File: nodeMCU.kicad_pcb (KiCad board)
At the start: 2 copper layers, 25.4 x 48.3 mm, 34 parts, among them J1 USB_B_Micro, J2 Conn_01x15, J3 Conn_01x15, Q1 S8050, Q2 S8050, SW1 RESET, SW2 FLASH, U1 AP1117-33, U2 CP2102N-A01-GQFN28, U3 ESP-12E

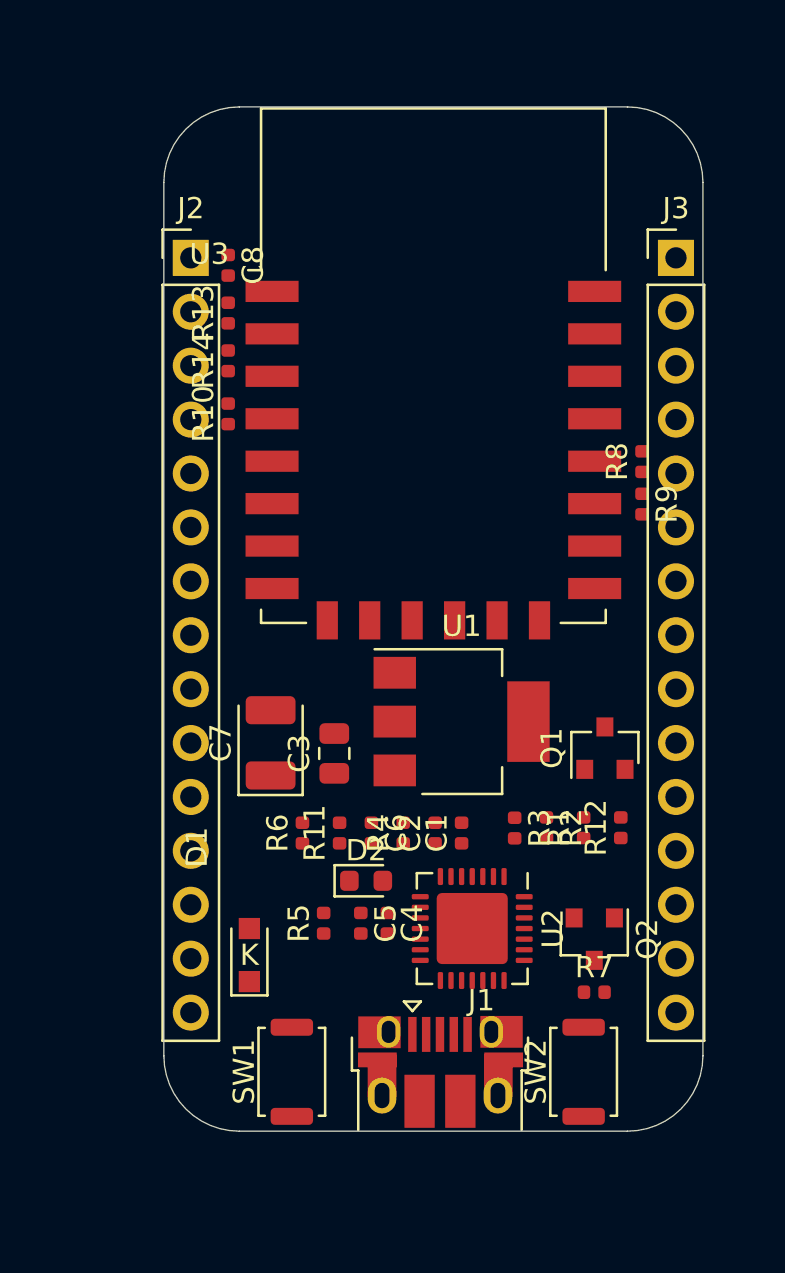
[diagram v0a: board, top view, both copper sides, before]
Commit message: Agrego agujeros de sujecion esquematico + pcb
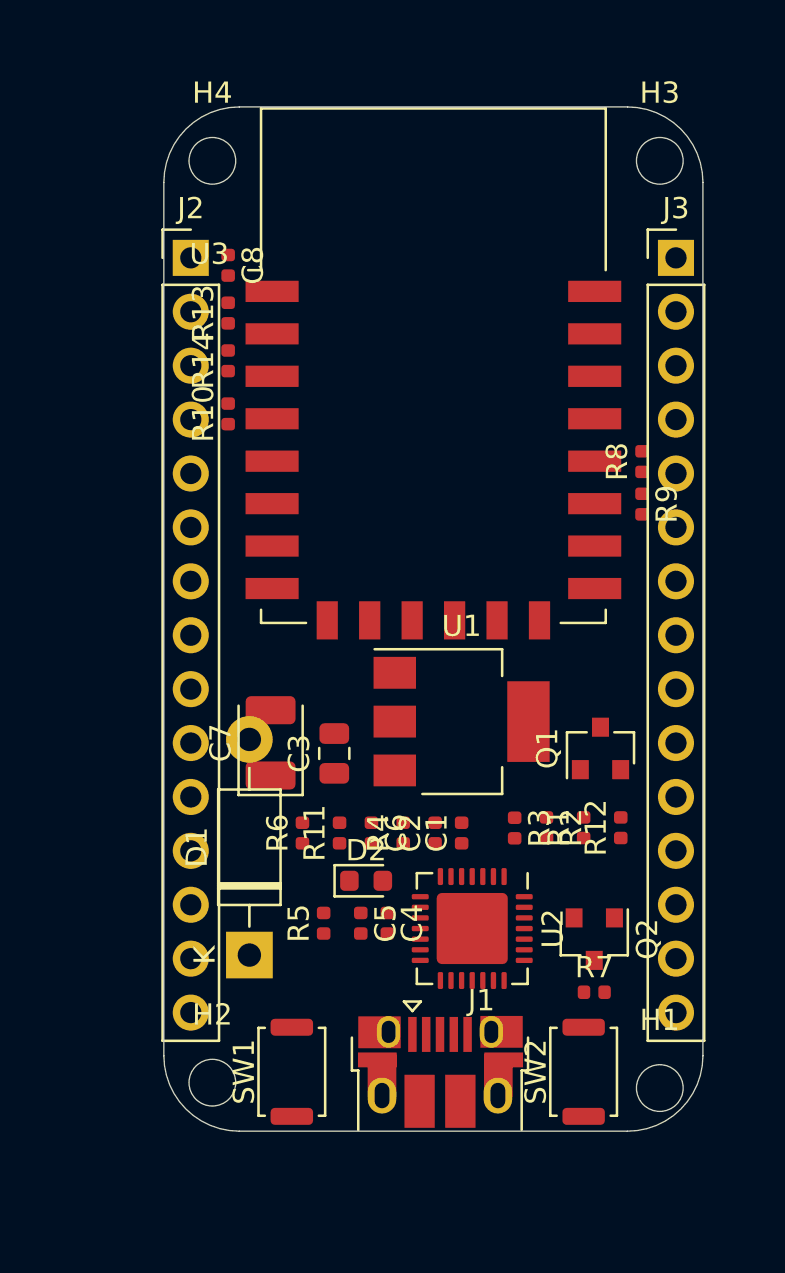
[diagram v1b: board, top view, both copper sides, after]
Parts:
- added H1: MountingHole, MountingHole:MountingHole_2.2mm_M2, F.Cu at (196.1, 96.3)
- added H2: MountingHole, MountingHole:MountingHole_2.2mm_M2, F.Cu at (175.0, 96.0)
- added H3: MountingHole, MountingHole:MountingHole_2.2mm_M2, F.Cu at (196.1, 52.6)
- added H4: MountingHole, MountingHole:MountingHole_2.2mm_M2, F.Cu at (175.0, 52.6)
- D1: footprint Diode_SMD:D_SOD-323_HandSoldering -> Diode_THT:D_DO-41_SOD81_P10.16mm_Horizontal
- moved Q1 0.21 mm to (193.3, 80.3)
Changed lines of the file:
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@@
     (tracks 0)
     (zones 0)
-    (modules 34)
+    (modules 38)
     (nets 56)
   )
@@
     )
   )
-  (module Diode_SMD:D_SOD-323_HandSoldering (layer F.Cu)
-    (at 176.75 90 90)
-    (descr SOD-323)
-    (tags SOD-323)
-    (attr smd)
-    (fp_text reference D1 (at 5.08 -2.47 90) (layer F.SilkS)
-      (effects (font (size 1 1) (thickness 0.15)))
-    )
-    (fp_text value 1N5819 (at 5.08 2.47 90) (layer F.Fab)
-      (effects (font (size 1 1) (thickness 0.15)))
-    )
-    (fp_line (start -1.9 -0.85) (end 1.25 -0.85) (layer F.SilkS) (width 0.12))
-    (fp_line (start -1.9 0.85) (end 1.25 0.85) (layer F.SilkS) (width 0.12))
-    (fp_line (start -2 -0.95) (end -2 0.95) (layer F.CrtYd) (width 0.05))
-    (fp_line (start -2 0.95) (end 2 0.95) (layer F.CrtYd) (width 0.05))
-    (fp_line (start 2 -0.95) (end 2 0.95) (layer F.CrtYd) (width 0.05))
-    (fp_line (start -2 -0.95) (end 2 -0.95) (layer F.CrtYd) (width 0.05))
-    (fp_line (start -0.9 -0.7) (end 0.9 -0.7) (layer F.Fab) (width 0.1))
-    (fp_line (start 0.9 -0.7) (end 0.9 0.7) (layer F.Fab) (width 0.1))
-    (fp_line (start 0.9 0.7) (end -0.9 0.7) (layer F.Fab) (width 0.1))
-    (fp_line (start -0.9 0.7) (end -0.9 -0.7) (layer F.Fab) (width 0.1))
-    (fp_line (start -0.3 -0.35) (end -0.3 0.35) (layer F.Fab) (width 0.1))
-    (fp_line (start -0.3 0) (end -0.5 0) (layer F.Fab) (width 0.1))
-    (fp_line (start -0.3 0) (end 0.2 -0.35) (layer F.Fab) (width 0.1))
-    (fp_line (start 0.2 -0.35) (end 0.2 0.35) (layer F.Fab) (width 0.1))
-    (fp_line (start 0.2 0.35) (end -0.3 0) (layer F.Fab) (width 0.1))
-    (fp_line (start 0.2 0) (end 0.45 0) (layer F.Fab) (width 0.1))
-    (fp_line (start -1.9 -0.85) (end -1.9 0.85) (layer F.SilkS) (width 0.12))
-    (fp_text user %R (at 5.47 0 90) (layer F.Fab)
-      (effects (font (size 1 1) (thickness 0.15)))
-    )
-    (fp_text user K (at 0 0) (layer F.SilkS)
-      (effects (font (size 1 1) (thickness 0.15)))
-    )
-    (pad 2 smd rect (at 1.25 0 90) (size 1 1) (layers F.Cu F.Paste F.Mask)
-      (net 4 VBUS))
-    (pad 1 smd rect (at -1.25 0 90) (size 1 1) (layers F.Cu F.Paste F.Mask)
-      (net 3 +5V))
-    (model ${KISYS3DMOD}/Diode_SMD.3dshapes/D_SOD-323.wrl
-      (at (xyz 0 0 0))
-      (scale (xyz 1 1 1))
-      (rotate (xyz 0 0 0))
-    )
-  )
   (module Capacitor_SMD:C_0402_1005Metric (layer F.Cu)
     (at 186.75 84.25 90)
@@
   )
   (module Package_TO_SOT_SMD:SOT-23 (layer F.Cu)
-    (at 193.5 80.25 90)
+    (at 193.294 80.264 90)
     (descr "SOT-23, Standard")
     (tags SOT-23)
@@
     )
   )
+  (module Diode_THT:D_DO-41_SOD81_P10.16mm_Horizontal (layer F.Cu)
+    (at 176.75 90 90)
+    (descr "Diode, DO-41_SOD81 series, Axial, Horizontal, pin pitch=10.16mm, , length*diameter=5.2*2.7mm^2, , http://www.diodes.com/_files/packages/DO-41%20(Plastic).pdf")
+    (tags "Diode DO-41_SOD81 series Axial Horizontal pin pitch 10.16mm  length 5.2mm diameter 2.7mm")
+    (fp_text reference D1 (at 5.08 -2.47 90) (layer F.SilkS)
+      (effects (font (size 1 1) (thickness 0.15)))
+    )
+    (fp_text value 1N5819 (at 5.08 2.47 90) (layer F.Fab)
+      (effects (font (size 1 1) (thickness 0.15)))
+    )
+    (fp_line (start 2.48 -1.35) (end 2.48 1.35) (layer F.Fab) (width 0.1))
+    (fp_line (start 2.48 1.35) (end 7.68 1.35) (layer F.Fab) (width 0.1))
+    (fp_line (start 7.68 1.35) (end 7.68 -1.35) (layer F.Fab) (width 0.1))
+    (fp_line (start 7.68 -1.35) (end 2.48 -1.35) (layer F.Fab) (width 0.1))
+    (fp_line (start 0 0) (end 2.48 0) (layer F.Fab) (width 0.1))
+    (fp_line (start 10.16 0) (end 7.68 0) (layer F.Fab) (width 0.1))
+    (fp_line (start 3.26 -1.35) (end 3.26 1.35) (layer F.Fab) (width 0.1))
+    (fp_line (start 3.36 -1.35) (end 3.36 1.35) (layer F.Fab) (width 0.1))
+    (fp_line (start 3.16 -1.35) (end 3.16 1.35) (layer F.Fab) (width 0.1))
+    (fp_line (start 2.36 -1.47) (end 2.36 1.47) (layer F.SilkS) (width 0.12))
+    (fp_line (start 2.36 1.47) (end 7.8 1.47) (layer F.SilkS) (width 0.12))
+    (fp_line (start 7.8 1.47) (end 7.8 -1.47) (layer F.SilkS) (width 0.12))
+    (fp_line (start 7.8 -1.47) (end 2.36 -1.47) (layer F.SilkS) (width 0.12))
+    (fp_line (start 1.34 0) (end 2.36 0) (layer F.SilkS) (width 0.12))
+    (fp_line (start 8.82 0) (end 7.8 0) (layer F.SilkS) (width 0.12))
+    (fp_line (start 3.26 -1.47) (end 3.26 1.47) (layer F.SilkS) (width 0.12))
+    (fp_line (start 3.38 -1.47) (end 3.38 1.47) (layer F.SilkS) (width 0.12))
+    (fp_line (start 3.14 -1.47) (end 3.14 1.47) (layer F.SilkS) (width 0.12))
+    (fp_line (start -1.35 -1.6) (end -1.35 1.6) (layer F.CrtYd) (width 0.05))
+    (fp_line (start -1.35 1.6) (end 11.51 1.6) (layer F.CrtYd) (width 0.05))
+    (fp_line (start 11.51 1.6) (end 11.51 -1.6) (layer F.CrtYd) (width 0.05))
+    (fp_line (start 11.51 -1.6) (end -1.35 -1.6) (layer F.CrtYd) (width 0.05))
+    (fp_text user %R (at 5.47 0 90) (layer F.Fab)
+      (effects (font (size 1 1) (thickness 0.15)))
+    )
+    (fp_text user K (at 0 -2.1 90) (layer F.Fab)
+      (effects (font (size 1 1) (thickness 0.15)))
+    )
+    (fp_text user K (at 0 -2.1 90) (layer F.SilkS)
+      (effects (font (size 1 1) (thickness 0.15)))
+    )
+    (pad 1 thru_hole rect (at 0 0 90) (size 2.2 2.2) (drill 1.1) (layers *.Cu *.Mask)
+      (net 3 +5V))
+    (pad 2 thru_hole oval (at 10.16 0 90) (size 2.2 2.2) (drill 1.1) (layers *.Cu *.Mask)
+      (net 4 VBUS))
+    (model ${KISYS3DMOD}/Diode_THT.3dshapes/D_DO-41_SOD81_P10.16mm_Horizontal.wrl
+      (at (xyz 0 0 0))
+      (scale (xyz 1 1 1))
+      (rotate (xyz 0 0 0))
+    )
+  )
+  (module MountingHole:MountingHole_2.2mm_M2 (layer F.Cu)
+    (at 196.088 96.266)
+    (descr "Mounting Hole 2.2mm, no annular, M2")
+    (tags "mounting hole 2.2mm no annular m2")
+    (attr virtual)
+    (fp_text reference H1 (at 0 -3.2) (layer F.SilkS)
+      (effects (font (size 1 1) (thickness 0.15)))
+    )
+    (fp_text value MountingHole (at 0 3.2) (layer F.Fab)
+      (effects (font (size 1 1) (thickness 0.15)))
+    )
+    (fp_text user %R (at 0.3 0) (layer F.Fab)
+      (effects (font (size 1 1) (thickness 0.15)))
+    )
+    (fp_circle (center 0 0) (end 2.2 0) (layer Cmts.User) (width 0.15))
+    (fp_circle (center 0 0) (end 2.45 0) (layer F.CrtYd) (width 0.05))
+    (pad 1 np_thru_hole circle (at 0 0) (size 2.2 2.2) (drill 2.2) (layers *.Cu *.Mask))
+  )
+  (module MountingHole:MountingHole_2.2mm_M2 (layer F.Cu)
+    (at 175.006 96.012)
+    (descr "Mounting Hole 2.2mm, no annular, M2")
+    (tags "mounting hole 2.2mm no annular m2")
+    (attr virtual)
+    (fp_text reference H2 (at 0 -3.2) (layer F.SilkS)
+      (effects (font (size 1 1) (thickness 0.15)))
+    )
+    (fp_text value MountingHole (at 0 3.2) (layer F.Fab)
+      (effects (font (size 1 1) (thickness 0.15)))
+    )
+    (fp_text user %R (at 0.3 0) (layer F.Fab)
+      (effects (font (size 1 1) (thickness 0.15)))
+    )
+    (fp_circle (center 0 0) (end 2.2 0) (layer Cmts.User) (width 0.15))
+    (fp_circle (center 0 0) (end 2.45 0) (layer F.CrtYd) (width 0.05))
+    (pad 1 np_thru_hole circle (at 0 0) (size 2.2 2.2) (drill 2.2) (layers *.Cu *.Mask))
+  )
+  (module MountingHole:MountingHole_2.2mm_M2 (layer F.Cu)
+    (at 196.088 52.578)
+    (descr "Mounting Hole 2.2mm, no annular, M2")
+    (tags "mounting hole 2.2mm no annular m2")
+    (attr virtual)
+    (fp_text reference H3 (at 0 -3.2) (layer F.SilkS)
+      (effects (font (size 1 1) (thickness 0.15)))
+    )
+    (fp_text value MountingHole (at 0 3.2) (layer F.Fab)
+      (effects (font (size 1 1) (thickness 0.15)))
+    )
+    (fp_circle (center 0 0) (end 2.45 0) (layer F.CrtYd) (width 0.05))
+    (fp_circle (center 0 0) (end 2.2 0) (layer Cmts.User) (width 0.15))
+    (fp_text user %R (at 0.3 0) (layer F.Fab)
+      (effects (font (size 1 1) (thickness 0.15)))
+    )
+    (pad 1 np_thru_hole circle (at 0 0) (size 2.2 2.2) (drill 2.2) (layers *.Cu *.Mask))
+  )
+  (module MountingHole:MountingHole_2.2mm_M2 (layer F.Cu)
+    (at 175.006 52.578)
+    (descr "Mounting Hole 2.2mm, no annular, M2")
+    (tags "mounting hole 2.2mm no annular m2")
+    (attr virtual)
+    (fp_text reference H4 (at 0 -3.2) (layer F.SilkS)
+      (effects (font (size 1 1) (thickness 0.15)))
+    )
+    (fp_text value MountingHole (at 0 3.2) (layer F.Fab)
+      (effects (font (size 1 1) (thickness 0.15)))
+    )
+    (fp_circle (center 0 0) (end 2.45 0) (layer F.CrtYd) (width 0.05))
+    (fp_circle (center 0 0) (end 2.2 0) (layer Cmts.User) (width 0.15))
+    (fp_text user %R (at 0.3 0) (layer F.Fab)
+      (effects (font (size 1 1) (thickness 0.15)))
+    )
+    (pad 1 np_thru_hole circle (at 0 0) (size 2.2 2.2) (drill 2.2) (layers *.Cu *.Mask))
+  )
   (gr_arc (start 194.564 94.742) (end 194.564 98.298) (angle -90) (layer Edge.Cuts) (width 0.05))

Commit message: Arreglo bordes de corte redondeados + ubico agujeros de sujecion
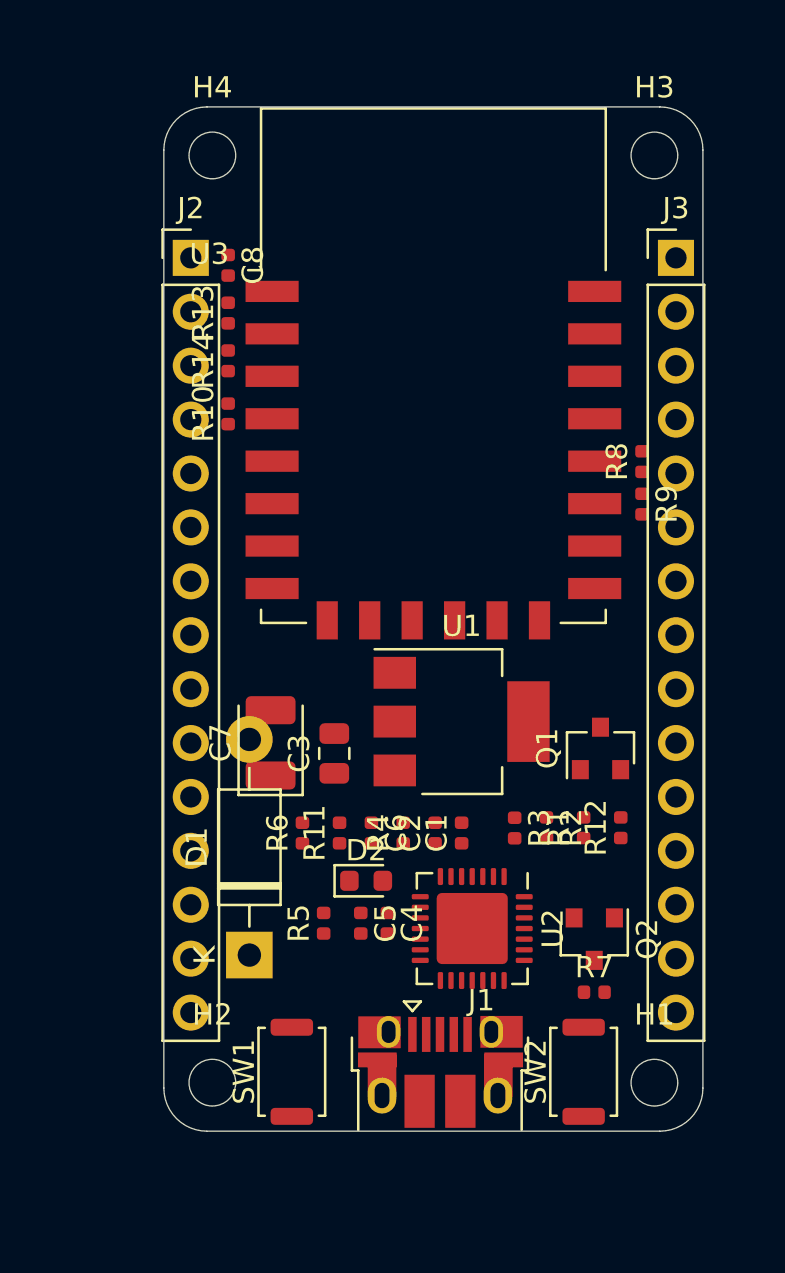
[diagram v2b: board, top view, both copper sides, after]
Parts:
- moved H1 0.36 mm to (195.8, 96.0)
- moved H3 0.36 mm to (195.8, 52.3)
- moved H4 0.25 mm to (175.0, 52.3)
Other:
- outline, holes or cut-outs redrawn
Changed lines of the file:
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@@
   )
   (module MountingHole:MountingHole_2.2mm_M2 (layer F.Cu)
-    (at 196.088 96.266)
+    (at 195.834 96.012)
     (descr "Mounting Hole 2.2mm, no annular, M2")
     (tags "mounting hole 2.2mm no annular m2")
@@
   )
   (module MountingHole:MountingHole_2.2mm_M2 (layer F.Cu)
-    (at 196.088 52.578)
+    (at 195.834 52.324)
     (descr "Mounting Hole 2.2mm, no annular, M2")
     (tags "mounting hole 2.2mm no annular m2")
@@
   )
   (module MountingHole:MountingHole_2.2mm_M2 (layer F.Cu)
-    (at 175.006 52.578)
+    (at 175.006 52.324)
     (descr "Mounting Hole 2.2mm, no annular, M2")
     (tags "mounting hole 2.2mm no annular m2")
@@
     (pad 1 np_thru_hole circle (at 0 0) (size 2.2 2.2) (drill 2.2) (layers *.Cu *.Mask))
   )
-  (gr_arc (start 194.564 94.742) (end 194.564 98.298) (angle -90) (layer Edge.Cuts) (width 0.05))
-  (gr_arc (start 176.276 94.742) (end 172.72 94.742) (angle -90) (layer Edge.Cuts) (width 0.05))
-  (gr_arc (start 194.564 53.594) (end 198.12 53.594) (angle -90) (layer Edge.Cuts) (width 0.05))
-  (gr_line (start 172.72 53.594) (end 172.72 94.742) (layer Edge.Cuts) (width 0.05))
-  (gr_line (start 176.276 50.038) (end 194.564 50.038) (layer Edge.Cuts) (width 0.05))
+  (gr_arc (start 174.752 52.07) (end 174.752 50.038) (angle -90) (layer Edge.Cuts) (width 0.05))
+  (gr_arc (start 196.088 52.07) (end 198.12 52.07) (angle -90) (layer Edge.Cuts) (width 0.05))
+  (gr_arc (start 196.088 96.266) (end 196.088 98.298) (angle -90) (layer Edge.Cuts) (width 0.05))
+  (gr_arc (start 174.752 96.266) (end 172.72 96.266) (angle -90) (layer Edge.Cuts) (width 0.05))
+  (gr_line (start 172.72 52.07) (end 172.72 96.266) (layer Edge.Cuts) (width 0.05))
+  (gr_line (start 174.752 50.038) (end 196.088 50.038) (layer Edge.Cuts) (width 0.05))
   (dimension 25.460071 (width 0.15) (layer Dwgs.User)
     (gr_text "25,460 mm" (at 185.411623 40.832851 359.8649748) (layer Dwgs.User)
@@
     (arrow2b (pts (xy 172.678559 42.102847) (xy 173.806442 41.519083)))
   )
-  (gr_arc (start 176.276 53.594) (end 176.276 50.038) (angle -90) (layer Edge.Cuts) (width 0.05))
-  (gr_line (start 194.564 98.298) (end 176.276 98.298) (layer Edge.Cuts) (width 0.05))
-  (gr_line (start 198.12 53.594) (end 198.12 94.742) (layer Edge.Cuts) (width 0.05))
+  (gr_line (start 196.088 98.298) (end 174.752 98.298) (layer Edge.Cuts) (width 0.05))
+  (gr_line (start 198.12 52.07) (end 198.12 96.266) (layer Edge.Cuts) (width 0.05))
   (dimension 48.26 (width 0.15) (layer Dwgs.User)
     (gr_text "48,260 mm" (at 203.23 74.168 270) (layer Dwgs.User)

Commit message: Comienzo el ruteo
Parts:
- D1: footprint Diode_THT:D_DO-41_SOD81_P10.16mm_Horizontal -> Diode_SMD:D_SOD-323_HandSoldering
- J2, J3: moved to B.Cu
- moved R10 20.0 mm to (176.2, 84.5), turned to 270 degrees
- moved C6 7.70 mm to (180.8, 76.8), turned to 0 degrees
- moved R7 7.26 mm to (192.7, 84.5), turned to 90 degrees
- moved R12 7.25 mm to (194.5, 76.8)
- moved R5 4.26 mm to (181.7, 84.5)
- moved R11 2.94 mm to (178.1, 84.5), turned to 270 degrees
- moved R1 2.06 mm to (194.5, 84.5)
- moved SW2 0.75 mm to (191.8, 95.5)
- moved R6 0.70 mm to (179.9, 84.5)
- moved R3 0.53 mm to (189.0, 84.5)
- moved C1 0.51 mm to (187.2, 84.5)
- moved R4 0.51 mm to (183.6, 84.5)
- moved R2 0.51 mm to (190.8, 84.5)
- moved SW1 0.50 mm to (179.2, 95.5)
- moved C7 0.35 mm to (177.5, 79.8), turned to 270 degrees
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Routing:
- net GND: track 0.00 -> 15.8 mm
- net +3V3: track 0.00 -> 6.36 mm
- net /ADC: track 0.00 -> 6.03 mm
- net Net-(Q2-Pad2): track 0.00 -> 3.62 mm
- net /nRST: track 0.00 -> 3.30 mm
- net /nRTS_CP: track 0.00 -> 3.14 mm
- net Net-(Q1-Pad2): track 0.00 -> 2.86 mm
- net +5V: track 0.00 -> 2.81 mm
- net /ADC_EX: track 0.00 -> 2.74 mm
